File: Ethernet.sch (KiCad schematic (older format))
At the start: 43 parts

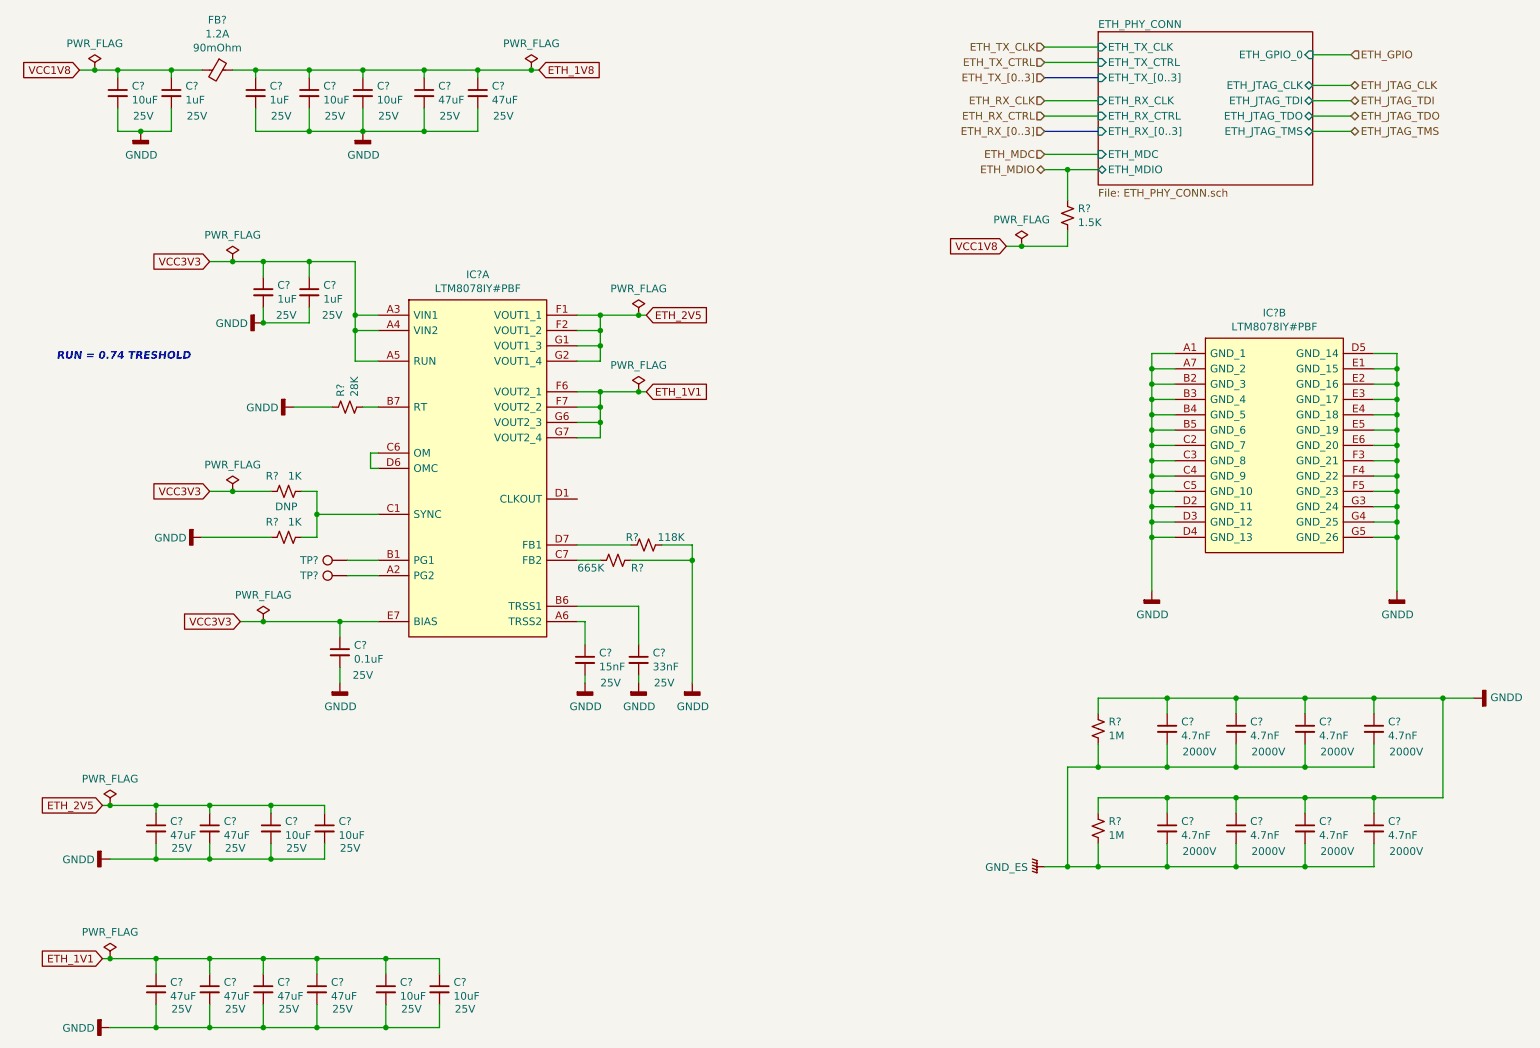
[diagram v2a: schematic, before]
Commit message: Connected Ethernet sheet with FPGA bank
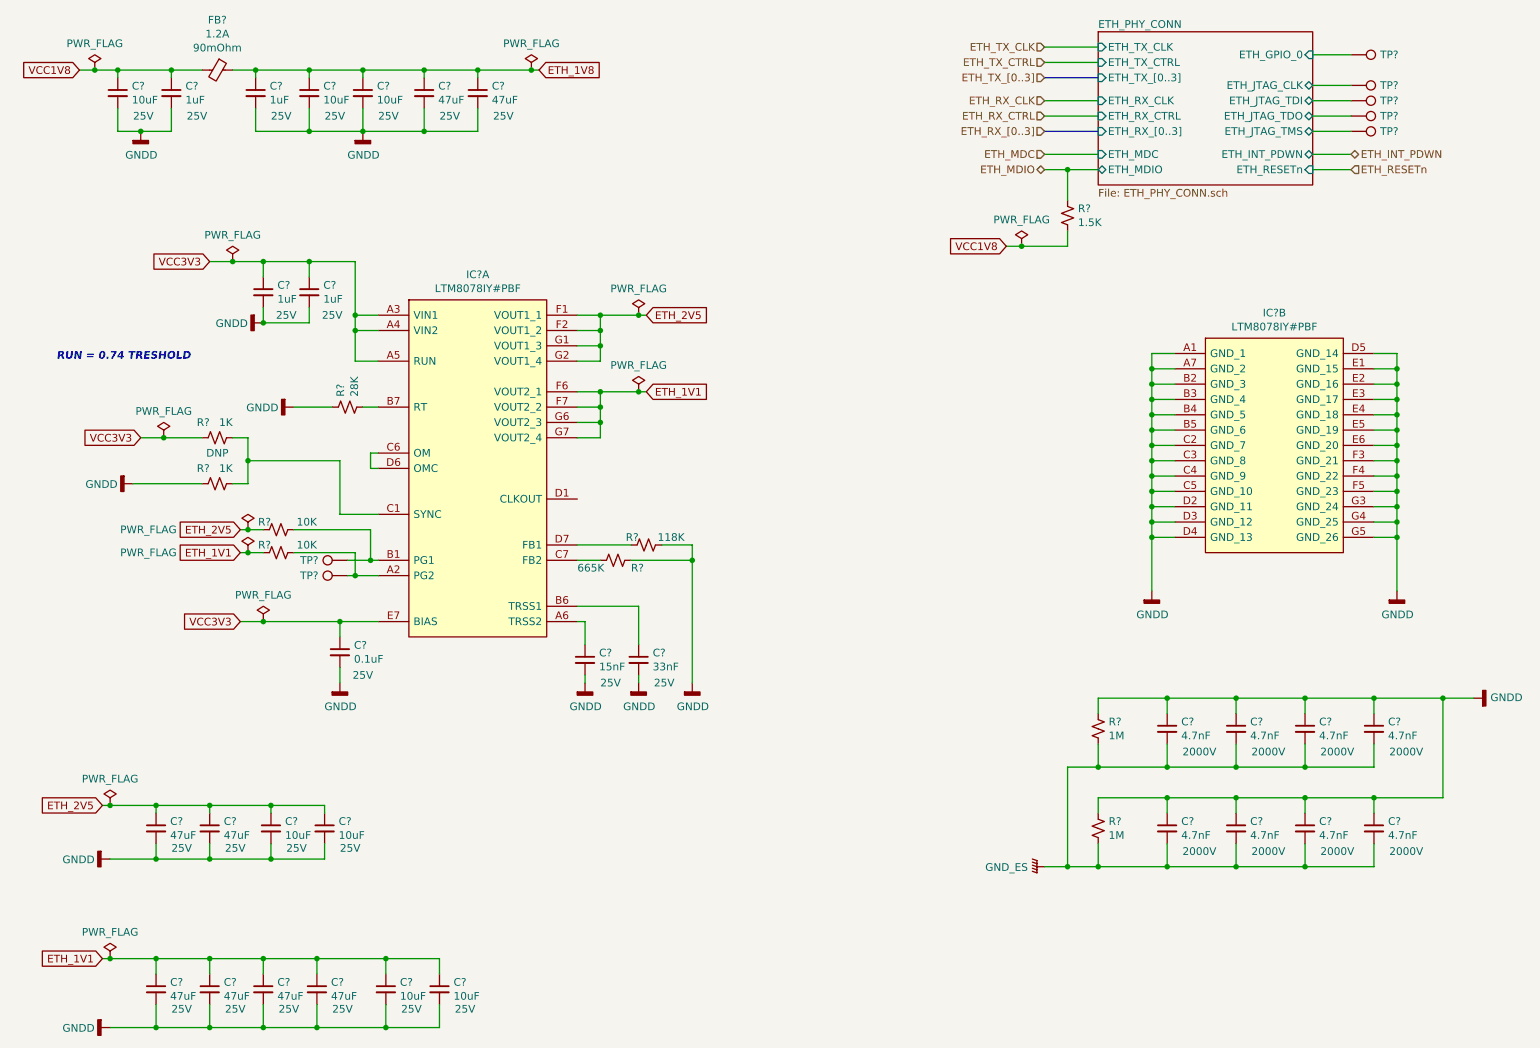
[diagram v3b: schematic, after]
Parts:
- added R? (x2): 10K, Resistor_SMD:R_0603_1608Metric_Pad0.98x0.95mm_HandSolder, symbol Device:R_Small_US
- added TP? (x5): TestPoint, TestPoint:TestPoint_Pad_D1.5mm, symbol Connector:TestPoint
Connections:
- net ETH_1V1: now also R?.1
- net ETH_2V5: now also R?.1
- net at IC?.A2 (PG2), TP?.1: now also R?.2
- net at IC?.B1 (PG1), TP?.1: now also R?.2
- new net ETH_PHY_CONN/ETH_GPIO_0: TP?.1
- new net ETH_PHY_CONN/ETH_JTAG_CLK: TP?.1
- new net ETH_PHY_CONN/ETH_JTAG_TDI: TP?.1
- new net ETH_PHY_CONN/ETH_JTAG_TDO: TP?.1
- new net ETH_PHY_CONN/ETH_JTAG_TMS: TP?.1
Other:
- moved on the sheet: R?

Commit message: PCB created and schematics annotated High speed connections added to the BTB
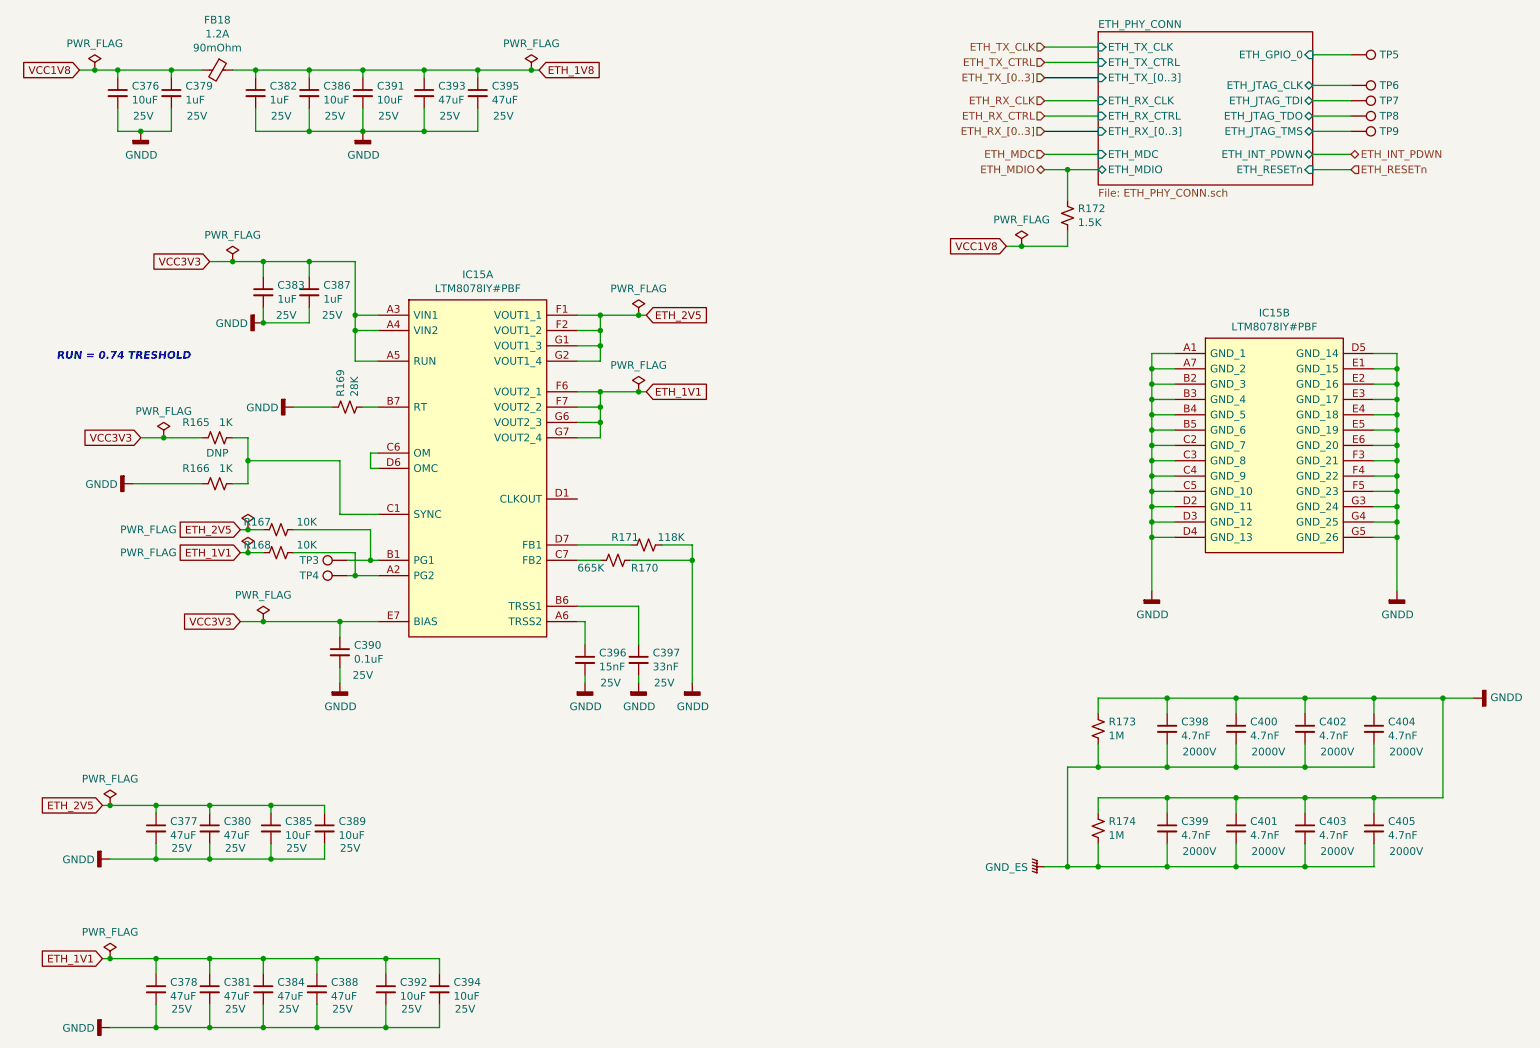
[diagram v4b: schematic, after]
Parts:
- gave numbers to parts that had none: 49

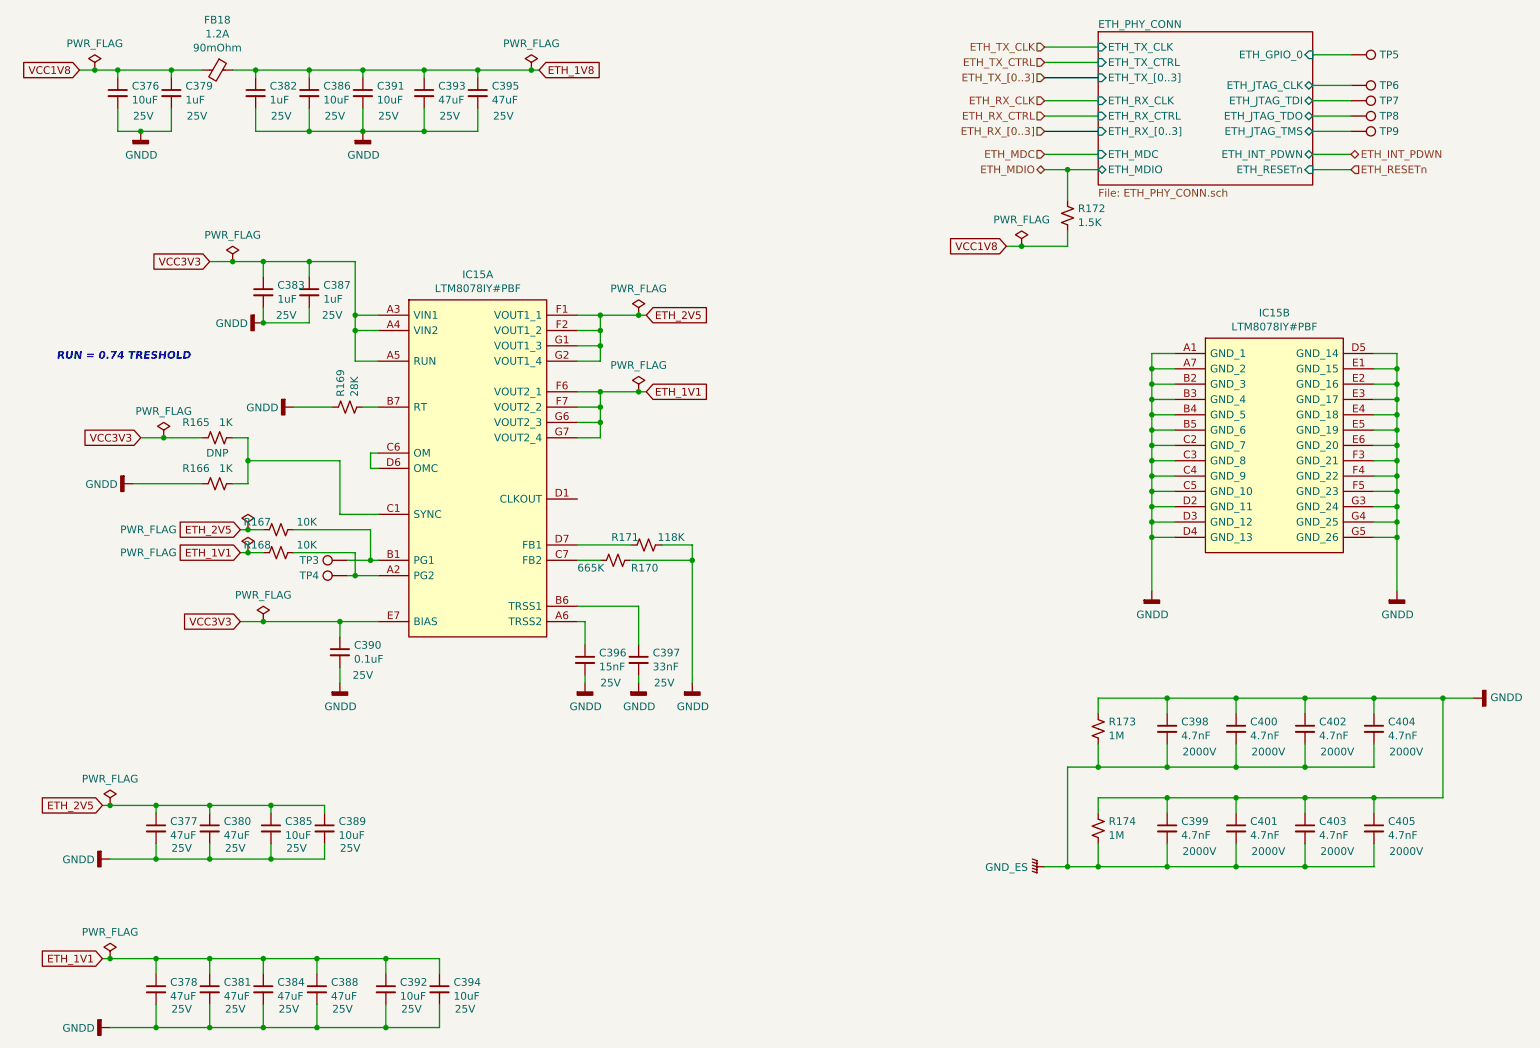
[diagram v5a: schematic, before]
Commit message: Corrected PCB import errors
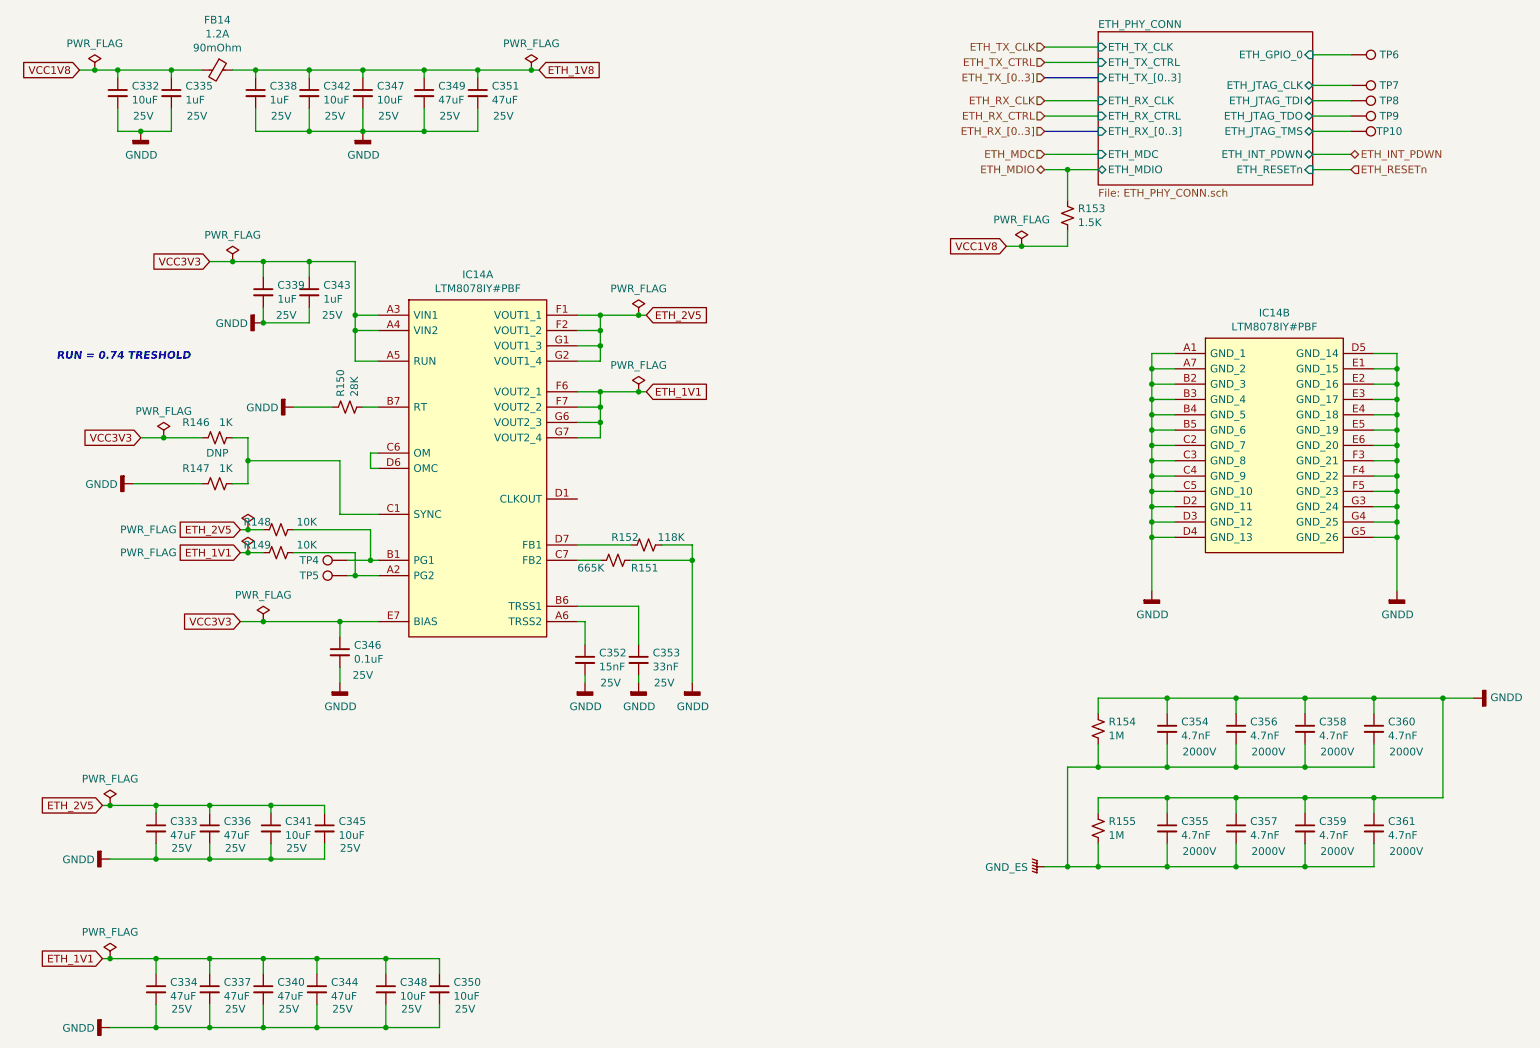
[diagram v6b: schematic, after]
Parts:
- renumbered C376 to C332, C377 to C333, C378 to C334, C379 to C335, C380 to C336, C381 to C337, C382 to C338, C383 to C339, C384 to C340, C385 to C341, C386 to C342, C387 to C343, C388 to C344, C389 to C345, C390 to C346, C391 to C347, C392 to C348, C393 to C349, C394 to C350, C395 to C351, C396 to C352, C397 to C353, C398 to C354, C399 to C355, C400 to C356, C401 to C357, C402 to C358, C403 to C359, C404 to C360, C405 to C361, FB18 to FB14, IC15 to IC14, R165 to R146, R166 to R147, R167 to R148, R168 to R149, R169 to R150, R170 to R151, R171 to R152, R172 to R153, R173 to R154, R174 to R155, TP9 to TP10, TP3 to TP4, TP4 to TP5, TP5 to TP6, TP6 to TP7, TP7 to TP8, TP8 to TP9
